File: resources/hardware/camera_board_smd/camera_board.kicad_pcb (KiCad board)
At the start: 2 copper layers, 10 parts, among them P1 CONN_01X02

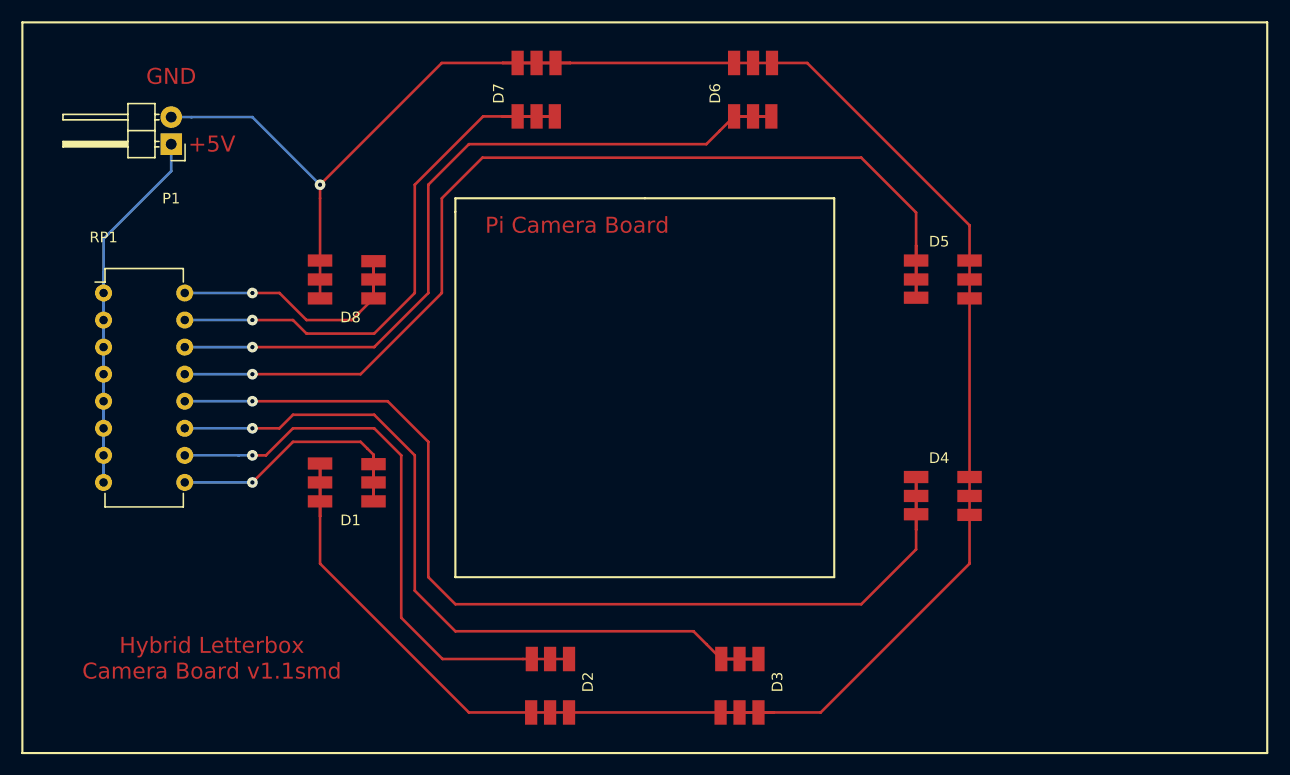
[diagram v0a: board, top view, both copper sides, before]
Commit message: added lasercut sketches for outer frame
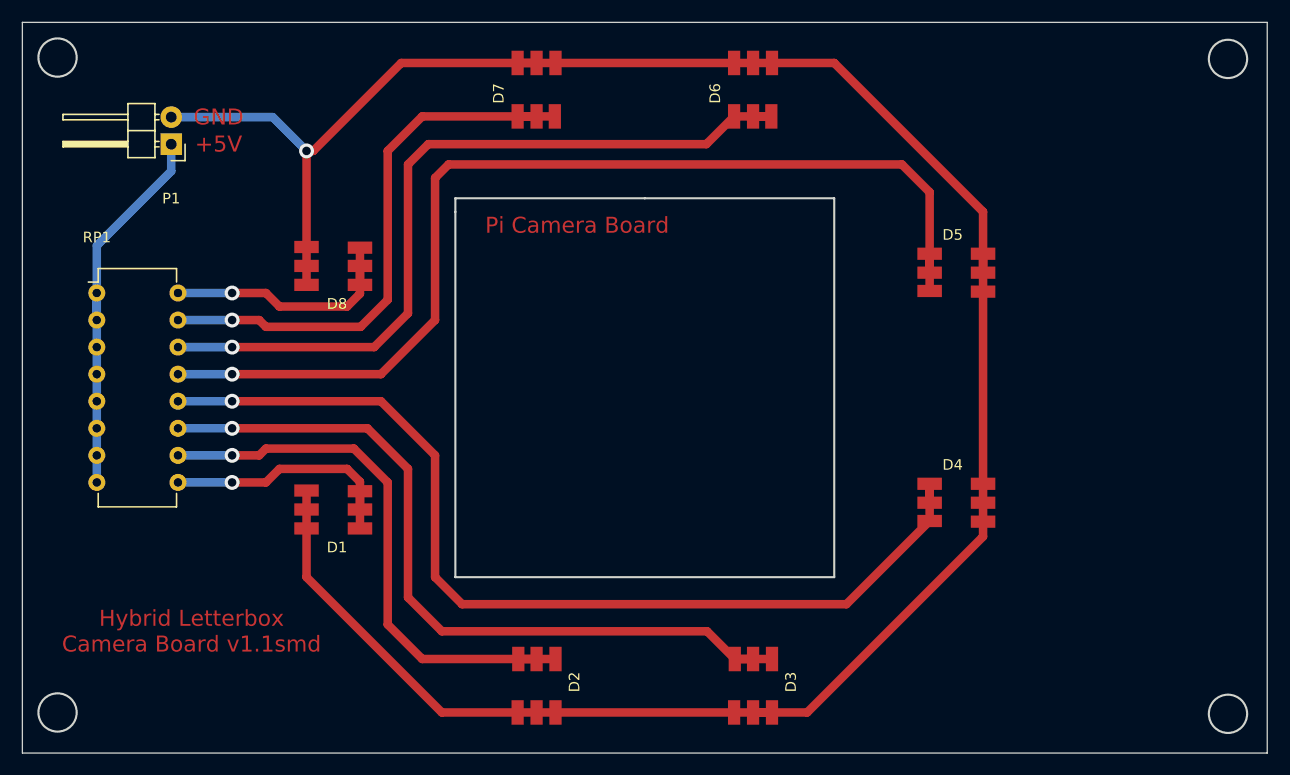
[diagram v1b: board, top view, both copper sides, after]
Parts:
- moved D1 2.84 mm to (115.6, 116.8)
- moved D8 1.80 mm to (115.6, 94.0)
- moved D4 1.42 mm to (174.0, 116.2)
- moved D5 1.42 mm to (174.0, 94.6)
- moved D3 1.27 mm to (154.9, 133.3)
- moved D2 1.27 mm to (134.6, 133.3)
- moved RP1 0.64 mm to (93.3, 96.5)
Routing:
- net +5V: track 54.1 -> 37.2 mm
- net GND: track 229.2 -> 218.8 mm
- net Net-(D1-Pad4): track 28.6 -> 24.2 mm
- net Net-(D4-Pad4): track 97.9 -> 93.6 mm
- net Net-(D7-Pad4): track 56.3 -> 53.8 mm
- net Net-(D8-Pad4): track 26.6 -> 24.2 mm
- net Net-(D2-Pad4): track 55.0 -> 53.4 mm
- net Net-(D5-Pad4): track 97.3 -> 98.6 mm
- net Net-(D3-Pad4): track 74.8 -> 73.5 mm
- net Net-(D6-Pad4): track 73.5 -> 74.6 mm
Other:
- board outline added: 116.8 x 68.6 mm
- net class Default: clearance 0.2 -> 0.8; trace_width 0.25 -> 0.8; via_dia 0.6 -> 1.4; via_drill 0.4 -> 0.8
- net class Standard removed
- rule trace_clearance: 0.2 -> 0.8
- rule trace_min: 0.2 -> 0.8
